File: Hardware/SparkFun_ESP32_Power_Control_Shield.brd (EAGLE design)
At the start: 101.6 x 50.8 mm, 67 parts, among them IC1 OP-AMP, IC2 OP-AMP, J1 5.5x2.1mm Barrel, U1 MC33926, U2 MC33926, U3 MC33926, U4 LM317

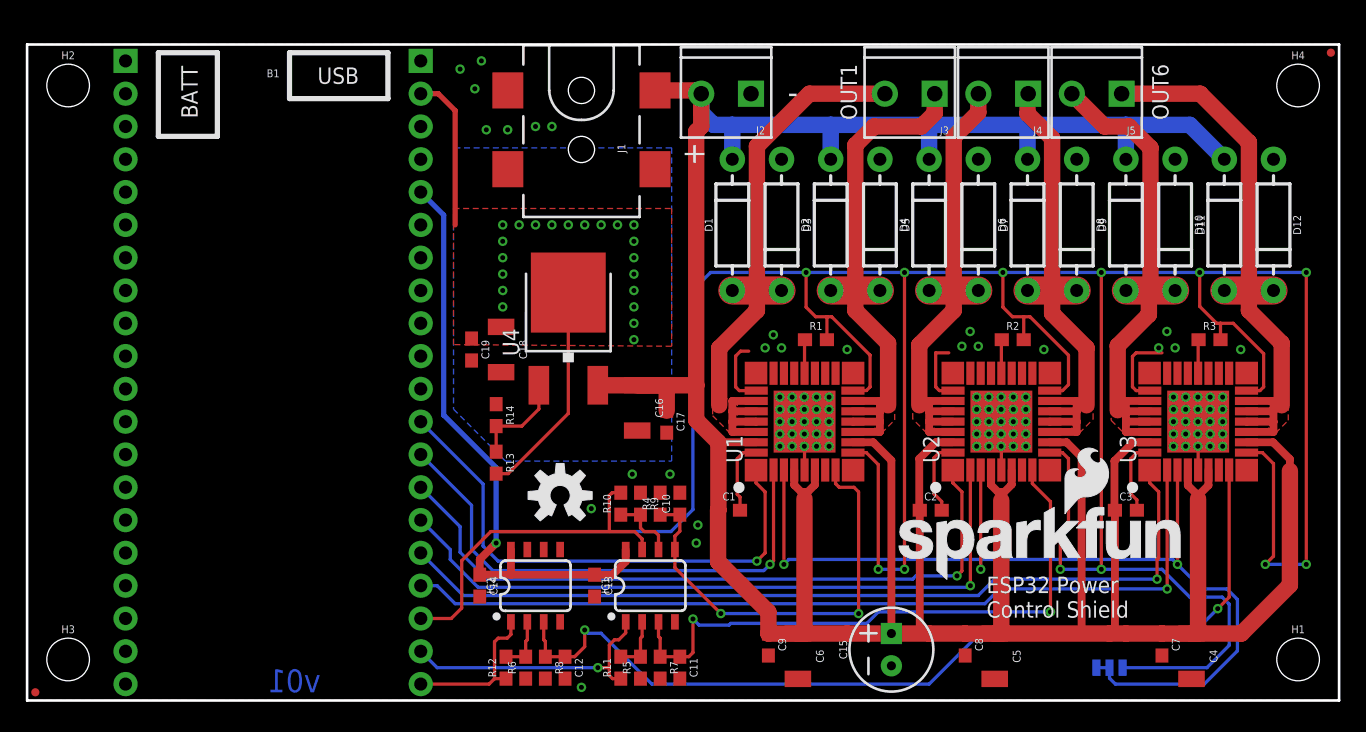
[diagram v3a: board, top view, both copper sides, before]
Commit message: Same changes as design review
Forgot to save changes before commit.
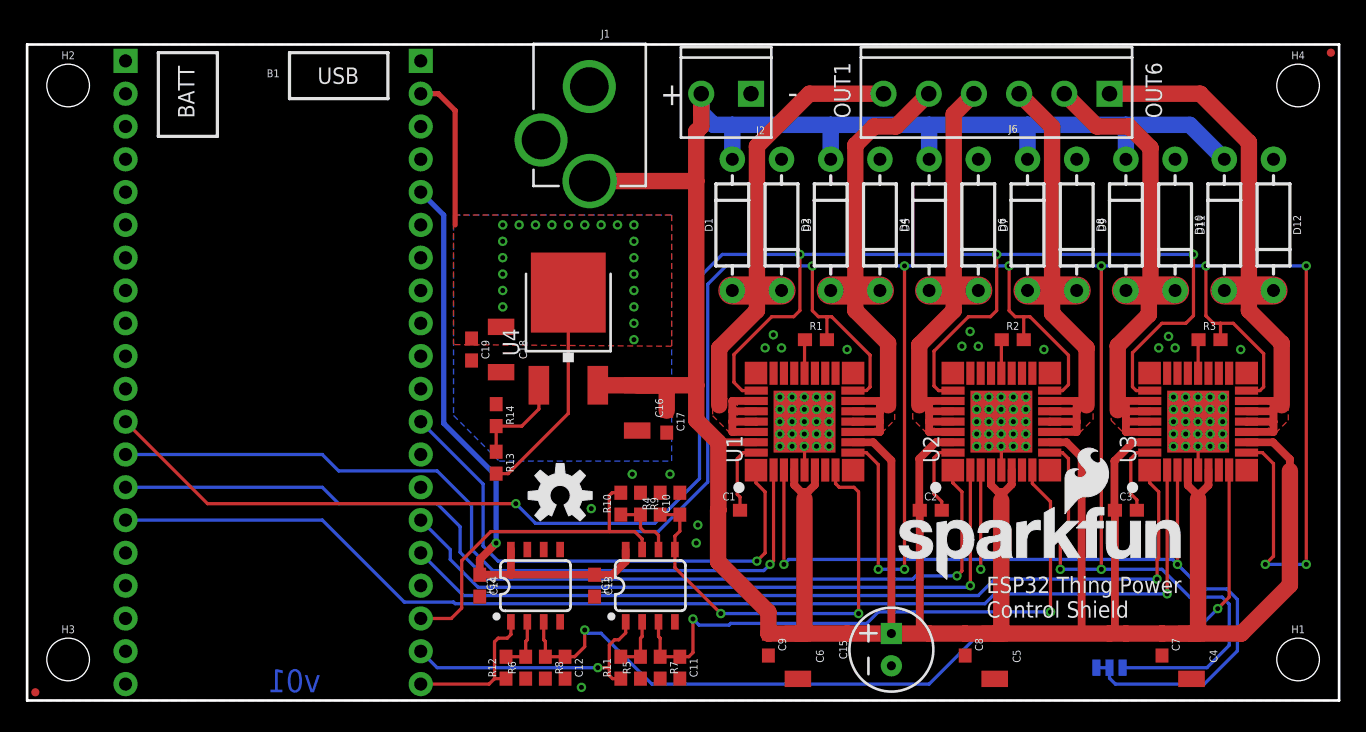
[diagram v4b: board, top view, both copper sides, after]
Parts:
- removed J3, J4, J5: (no value), SparkFun-Connectors:SCREWTERMINAL-3.5MM-2_LOCK
- added J6: (no value), SparkFun-Connectors:SCREWTERMINAL-3.5MM-6
- J1: value 5.5x2.1mm Barrel -> POWER_JACKPTH_LOCK; device SparkFun-Connectors:POWER_JACK_SMD -> SparkFun-Connectors:POWER_JACK_PTH_LOCK
- moved J1 6.89 mm to (43.6, 54.1), turned to 180 degrees
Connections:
- new net D1: B1.29, U1.P$26, U2.P$26, U3.P$26
- net CTRL_2: now also B1.28; no longer B1.13
- net CTRL_3: now also B1.27; no longer B1.14
- net CTRL_6: now also B1.26; no longer B1.17
- net GND: now also J1.GNDBREAK; no longer J1.P$4, U1.P$26, U2.P$26, U3.P$26
- net P_OUT1: now also J6.6; no longer J3.2
- net P_OUT2: now also J6.5; no longer J3.1
- net P_OUT3: now also J6.4; no longer J4.2
- net P_OUT4: now also J6.3; no longer J4.1
- net P_OUT5: now also J6.2; no longer J5.2
- net P_OUT6: now also J6.1; no longer J5.1
- net VCC: now also J1.PWR; no longer J1.VIN0
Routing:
- net D1: track 0.00 -> 148.3 mm, vias 0 -> 4
- net CTRL_6: track 68.1 -> 93.3 mm
- net CTRL_3: track 54.4 -> 77.2 mm
- net CTRL_2: track 40.4 -> 63.3 mm
- net GND: track 25.0 -> 8.40 mm, vias 100 -> 93
- net VCC: track 295.8 -> 300.7 mm
- net 3.3V: track 304.0 -> 305.6 mm
- net P_OUT2: track 44.5 -> 43.1 mm
- net P_OUT6: track 47.4 -> 48.3 mm
- net P_OUT5: track 42.8 -> 43.4 mm
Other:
- board text added: "Disable Outputs (5)"
- board text added: "ESP32 Thing Power Control Shield"
- board text added: "Output 1 (25)"
- board text added: "Output 2 (18)"
- board text added: "Output 3 (23)"
- board text added: "Output 4 (33)"
- board text added: "Output 5 (32)"
- board text added: "Output 6 (19)"
- board text removed: "25"
- board text removed: "32"
- board text removed: "34"
- board text removed: "35"
- board text removed: "39"
- board text removed: "ESP32 Power Control Shield"
- board text removed: "IO PIN"

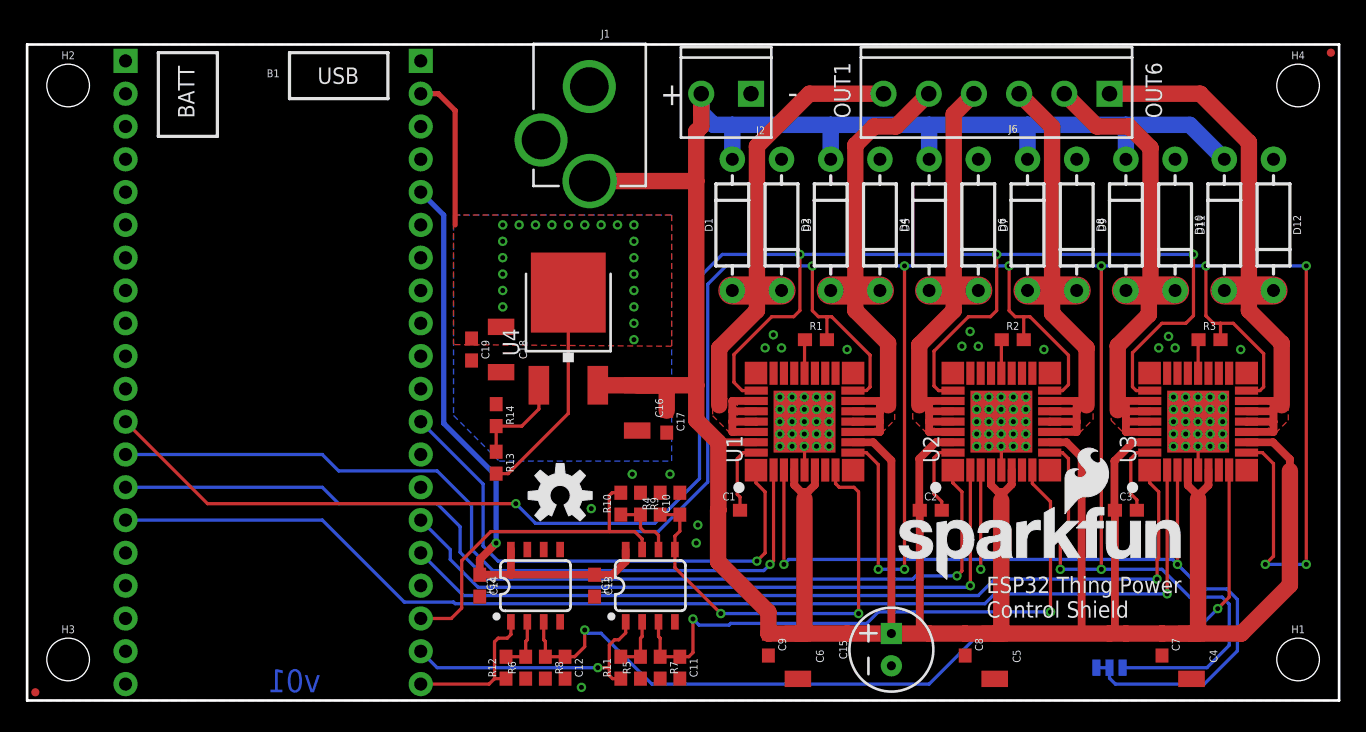
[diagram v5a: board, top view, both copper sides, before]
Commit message: v10 Changes
- Flipped connectors from top layer to bottom
- Replaced 2-pin power connector with a 3-pin. Additional pin breaks out
5V power rail for a 5VDC fan.
- Added pull-down resistor to disable output (enabled by default).
- Replaced 5V LDO with DC/DC converter
- Replaced 240ohm resistors with 220ohm
- Replaced 15k feedback resistors with solder jumper and unpopulated PTH
resistor
- Increased trace width on VCC rail
- Added 5V bypass jumper to bypass the DC/DC converter which has a
minimum input voltage of 7V.
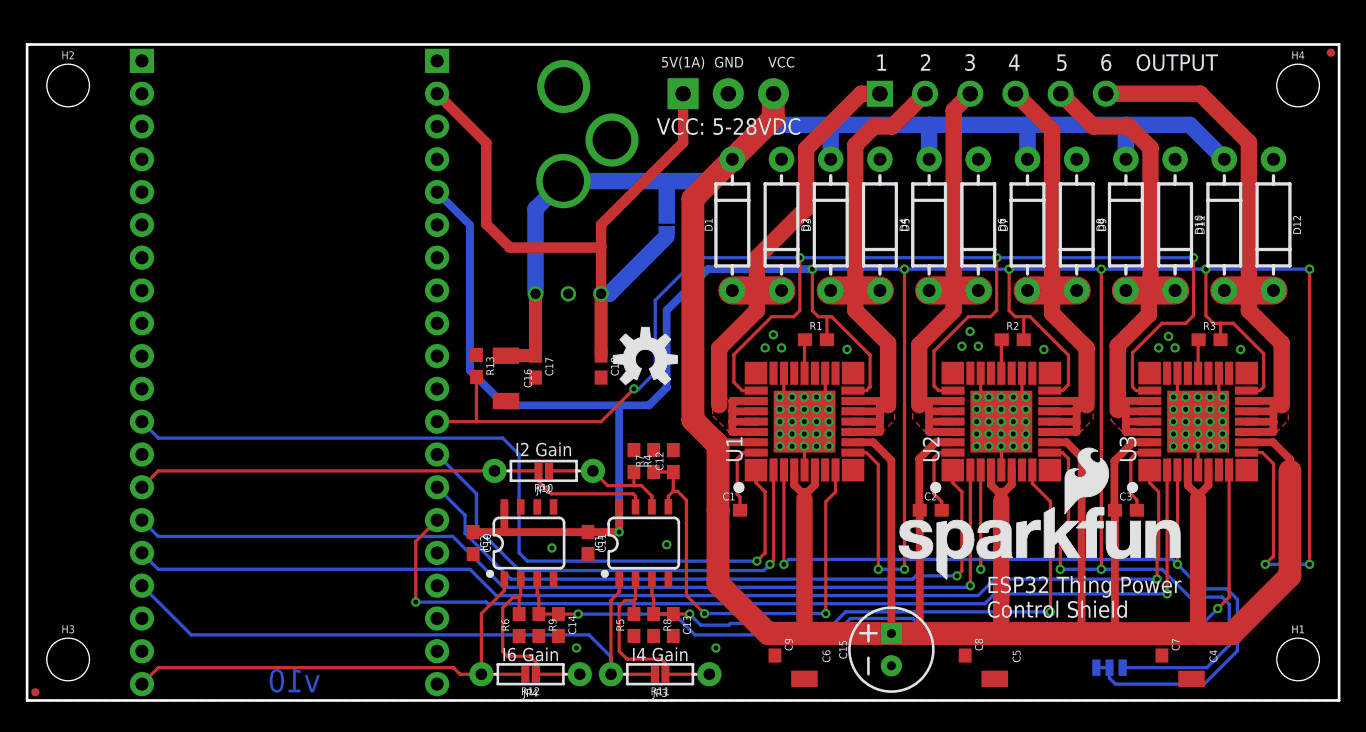
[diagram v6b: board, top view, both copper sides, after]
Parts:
- removed C19: 0.1uF, SparkFun-Capacitors:0603
- removed J6: (no value), SparkFun-Connectors:SCREWTERMINAL-3.5MM-6
- removed R14: 715, SparkFun-Resistors:0603
- added J3: (no value), SparkFun-Connectors:SCREWTERMINAL-3.5MM-3
- added JP2, JP3, JP4: (no value), SparkFun-Jumpers:SMT-JUMPER_2_NC_PASTE_NO-SILK
- added JP5: 5V Bypass, SparkFun-Jumpers:SMT-JUMPER_2_NO_SILK
- added U$1: (no value), SparkFun-Aesthetics:ORDERING_INSTRUCTIONS
- C10, C11: value 1.0uF -> 0.1uF
- C13, C14: value 0.1uF -> 1.0uF
- C18: value 10uF -> 0.1uF; device SparkFun-Capacitors:1210 -> SparkFun-Capacitors:0603
- J1: value POWER_JACKPTH_LOCK -> (none); device SparkFun-Connectors:POWER_JACK_PTH_LOCK -> SparkFun-Connectors:SCREWTERMINAL-3.5MM-6
- J2: value (none) -> POWER_JACKPTH_LOCK; device SparkFun-Connectors:SCREWTERMINAL-3.5MM-2_LOCK -> SparkFun-Connectors:POWER_JACK_PTH_LOCK
- R10, R11, R12: value 15k -> (none); device SparkFun-Resistors:0603 -> SparkFun-Resistors:AXIAL-0.3
- R13, R4: value 240 -> 10k
- R7, R8: value 240 -> 220
- R9: value 10k -> 220
- U4: value LM317 -> R-78E5.0-1.0; device SparkFun-IC-Power:V-REG_DPACK -> SparkFun-IC-Power:DC-DC_CONVERTER_78XX
- moved B1 24.1 mm to (7.62, 50.8), flipped to the bottom
- moved J1 23.6 mm to (66.0, 47.0), flipped to the bottom
- moved C12 18.1 mm to (50.0, 18.5), turned to 90 degrees
- moved C10 16.3 mm to (34.5, 12.2), turned to 270 degrees
- moved J2 16.0 mm to (41.5, 54.1), flipped to the bottom
- moved R7 16.0 mm to (48.5, 18.5), turned to 90 degrees
- moved LOGO2 12.4 mm to (47.9, 26.4)
- moved R9 12.3 mm to (39.6, 5.84)
- moved C11 12.0 mm to (43.4, 12.2)
- moved C17 11.0 mm to (39.4, 25.9)
- moved C16 10.4 mm to (37.1, 24.9)
- moved R8 9.01 mm to (48.5, 5.84)
- moved C18 7.86 mm to (44.5, 25.9)
- moved R13 7.65 mm to (34.8, 25.9)
- moved C14 6.82 mm to (41.1, 5.84)
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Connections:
- removed net ADJ: R13.1, R14.2, U4.1
- net 3.3V: now also B1.36, C10.1, C11.1; no longer B1.5, C13.1, C14.1
- net 5V: now also B1.39, J3.1, JP5.2, U4.VOUT; no longer B1.2, C19.1, R13.2, U4.4
- net D1: now also R13.2
- net FB2: now also B1.14, JP2.2, R10.P$2; no longer B1.18, R10.2
- net FB4: now also B1.17, JP3.2, R11.P$2; no longer B1.19, R11.1
- net FB6: now also JP4.2, R12.P$2; no longer R12.1
- net GND: now also J2.GND, J2.GNDBREAK, J3.2, R13.1, R4.1, R9.2, U4.GND; no longer C19.2, J1.GND, J1.GNDBREAK, J2.1, R14.1, R4.2, R9.1
- net I_SENSE1: now also C12.1, R7.1; no longer C10.1, R4.1
- net I_SENSE2: now also C13.1, R8.1; no longer C11.1, R7.1
- net I_SENSE3: now also C14.1, R9.1; no longer C12.1, R8.1
- net N$2: now also JP2.1, R10.P$1, R4.2; no longer R10.1, R9.2
- net N$4: now also JP4.1, R12.P$1; no longer R12.2
- net N$5: now also JP3.1, R11.P$1; no longer R11.2
- net P_OUT1: now also J1.1; no longer J6.6
- net P_OUT2: now also J1.2; no longer J6.5
- net P_OUT3: now also J1.3; no longer J6.4
- net P_OUT4: now also J1.4; no longer J6.3
- net P_OUT5: now also J1.5; no longer J6.2
- net P_OUT6: now also J1.6; no longer J6.1
- net VCC: now also J2.PWR, J3.3, JP5.1, U4.VIN; no longer J1.PWR, J2.2, U4.3
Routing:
- net D1: track 148.3 -> 114.4 mm
- net FB4: track 21.0 -> 51.0 mm, vias 1 -> 0
- net GND: track 8.40 -> 38.4 mm, vias 93 -> 91
- net FB6: track 12.1 -> 38.5 mm
- net CTRL_2: track 63.3 -> 38.7 mm
- net CTRL_3: track 77.2 -> 52.8 mm
- net CTRL_1: track 40.9 -> 64.2 mm
- net 5V: track 28.9 -> 51.6 mm, vias 21 -> 0
- net CTRL_5: track 67.7 -> 89.3 mm
- net CTRL_4: track 54.2 -> 75.3 mm
- net CTRL_6: track 93.3 -> 75.2 mm, vias 1 -> 2
- net 3.3V: track 305.6 -> 290.8 mm
- net FB2: track 26.9 -> 40.9 mm
- net N$5: track 4.28 -> 15.8 mm
- net N$4: track 4.28 -> 15.0 mm
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- removed copper zone on layer 1, net 5V
- removed copper zone on layer 16, net 5V
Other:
- board text added: "5V"
- board text added: "5V(1A)"
- board text added: "BYPASS"
- board text added: "Copper Weight - 2 Ounce"
- board text added: "I-Sense 2 (34)"
- board text added: "I-Sense 4 (39)"
- board text added: "I2 Gain"
- board text added: "I4 Gain"
- board text added: "I6 Gain"
- board text added: "Out 1 (25)"
- board text added: "Out 2 (18)"
- board text added: "Out 3 (23)"
- board text added: "Out 4 (33)"
- board text added: "Out 5 (32)"
- board text added: "Out 6 (19)"
- board text added: "VCC: 5-28VDC"
- board text added: "v10"
- board text removed: "+"
- board text removed: "-"
- board text removed: "5-28VDC"
- board text removed: "I-Sense 2 (38)"
- board text removed: "I-Sense 4 (37)"
- board text removed: "Output 1 (25)"
- board text removed: "Output 2 (18)"
- board text removed: "Output 3 (23)"
- board text removed: "Output 4 (33)"
- board text removed: "Output 5 (32)"
- board text removed: "Output 6 (19)"
- board text removed: "v01"
